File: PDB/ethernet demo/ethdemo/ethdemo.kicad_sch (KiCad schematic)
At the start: 0 parts

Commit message: ad microcontroller and POE+ to demo
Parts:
- added C1: 4.7uF, Capacitor_SMD:C_0603_1608Metric, symbol Device:C
- added C2, C3, C4, C5, C6, C7: 100nF, Capacitor_SMD:C_0603_1608Metric, symbol Device:C
- added C8, C9: 2.2uF, Capacitor_SMD:C_0603_1608Metric, symbol Device:C
- added C83, C84: 0.1uF, Capacitor_SMD:C_0603_1608Metric, symbol Device:C
- added C85: 0.1uF, symbol Device:C
- added C86: 100nf, Capacitor_SMD:C_0603_1608Metric, symbol Device:C
- added D1, D2, D3, D4, D5: LED, LED_SMD:LED_0805_2012Metric, symbol Device:LED
- added D24: 100V, symbol Device:D_Zener
- added D25: 60V, symbol Device:D_Zener
- added F7: Fuse, Fuse:Fuse_1206_3216Metric, symbol Device:Fuse
- added J14: RJ45_Abracon_ARJP11A-MASA-B-A-EMU2, Connector_RJ:RJ45_Abracon_ARJP11A-MA_Horizontal, symbol Connector:RJ45_Abracon_ARJP11A-MASA-B-A-EMU2
- added Q13: CSD19538Q3AT, foot:CSD19538Q3AT, symbol sym&foot:CSD19538Q3AT
- added R10, R6, R7, R8, R9: 270, Resistor_SMD:R_0603_1608Metric, symbol Device:R
- added R73: 22.1Ohm, Resistor_SMD:R_0603_1608Metric, symbol Device:R
- added R74, R75, R76, R77: 1Ohm, Resistor_SMD:R_0603_1608Metric, symbol Device:R
- added R78: 47Ohm, Resistor_SMD:R_0603_1608Metric, symbol Device:R
- added TP1, TP2, TP3, TP4: TestPoint, TestPoint:TestPoint_Pad_D2.5mm, symbol Connector:TestPoint
- added U1: STM32H742VGTx, Package_QFP:LQFP-100_14x14mm_P0.5mm, symbol MCU_ST_STM32H7:STM32H742VGTx
- added U2, U3: LT1117-ADJ, symbol Regulator_Linear:LT1117-ADJ
- added U23: TPS23861PWR, foot:TPS23861PWR, symbol sym&foot:TPS23861PWR
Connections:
- new net: Q13.1 (S_1), Q13.2 (S_2), Q13.3 (S_3), R73.1, R74.1, R75.1, R76.1, R77.1
- new net: R10.1, U1.52 (PB13)
- new net: D5.2 (A), R10.2
- new net: R8.1, U1.45 (PE15)
- new net: D3.2 (A), R8.2
- new net: C85.2, D24.1 (K), D25.2 (A), F7.1, J14.10 (V-), TP4.1
- new net: R6.1, U1.43 (PE13)
- new net: D1.2 (A), R6.2
- new net: R7.1, U1.44 (PE14)
- new net: C8.2, U1.48 (VCAP)
- new net: R9.1, U1.51 (PB12)
- new net: C9.2, U1.73 (VCAP)
- new net: R73.2, U23.15 (SEN1)
- new net: D2.2 (A), R7.2
- new net: C86.2, J14.7
- new net: D4.2 (A), R9.2
- new net: C83.1, U23.1 (VDD), U23.2 (~{RESET}), U23.24 (~{SHTDWN})
- new net: F7.2, Q13.5 (D_1), Q13.6 (D_2), Q13.7 (D_3), Q13.8 (D_4), Q13.D1 (D_5), Q13.D2 (D_6), Q13.D3 (D_7), R78.1
- new net: R78.2, U23.16 (DRAIN1)
- new net: Q13.4 (G), U23.17 (GATE1)
- new net +3.3V: C1.1, C2.1, C3.2, C4.1, C5.1, C6.1, C7.1, TP2.1, U1.100 (VDD), U1.11 (VDD), U1.20 (VREF+), U1.21 (VDDA), U1.27 (VDD), U1.50 (VDD), U1.75 (VDD)
- new net 48V: C84.2, C85.1, D25.1 (K), J14.9 (V+), TP3.1, U23.28 (VPWR)
- new net BOOT0: U1.94 (BOOT0)
- new net CS: U1.28 (PA4)
- new net D+: U1.71 (PA12)
- new net D-: U1.70 (PA11)
- new net GND: C1.2, C2.2, C3.1, C4.2, C5.2, C6.2, C7.2, C8.1, C83.2, C84.1, C86.1, C9.1, D1.1 (K), D2.1 (K), D24.2 (A), D3.1 (K), D4.1 (K), D5.1 (K), R74.2, R75.2, R76.2, R77.2, TP1.1, U1.10 (VSS), U1.19 (VSSA), U1.26 (VSS), U1.49 (VSS), U1.74 (VSS), U1.99 (VSS), U23.11 (KSENSB), U23.12 (SEN4), U23.13 (DRAIN4), U23.18 (KSENSA), U23.19 (SEN2), U23.20 (DRAIN2), U23.22 (AGND), U23.23 (A3), U23.3 (SCL), U23.4 (SDAI), U23.7 (DGND), U23.8 (SEN3), U23.9 (DRAIN3)
- new net INT: U1.67 (PA8)
- new net MISO: U1.30 (PA6)
- new net MOSI: U1.31 (PA7)
- new net PA3: U1.25 (PA3)
- new net PB0: U1.34 (PB0)
- new net PB1: U1.35 (PB1)
- new net PB10: U1.46 (PB10)
- new net PB11: U1.47 (PB11)
- new net PB2: U1.36 (PB2)
- new net PC0: U1.15 (PC0)
- new net PC10: U1.78 (PC10)
- new net PC11: U1.79 (PC11)
- new net PC12: U1.80 (PC12)
- new net PC2: U1.17 (PC2_C)
- new net PC3: U1.18 (PC3_C)
- new net PC4: U1.32 (PC4)
- new net PC5: U1.33 (PC5)
- new net PC8: U1.65 (PC8)
- new net PC9: U1.66 (PC9)
- new net PD2: U1.83 (PD2)
- new net PE11: U1.41 (PE11)
- new net PE12: U1.42 (PE12)
- new net PE7: U1.37 (PE7)
- new net PE8: U1.38 (PE8)
- new net PE9: U1.39 (PE9)
- new net RST: U1.68 (PA9)
- new net SCK: U1.29 (PA5)
- new net SWCLK: U1.76 (PA14)
- new net SWDIO: U1.72 (PA13)
- new net SWO/TRACE: U1.89 (PB3)
- new net UART4_RX: U1.23 (PA1)
- new net UART4_TX: U1.22 (PA0)
- no-connect marks 0 -> 56
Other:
- note added: "TBD"

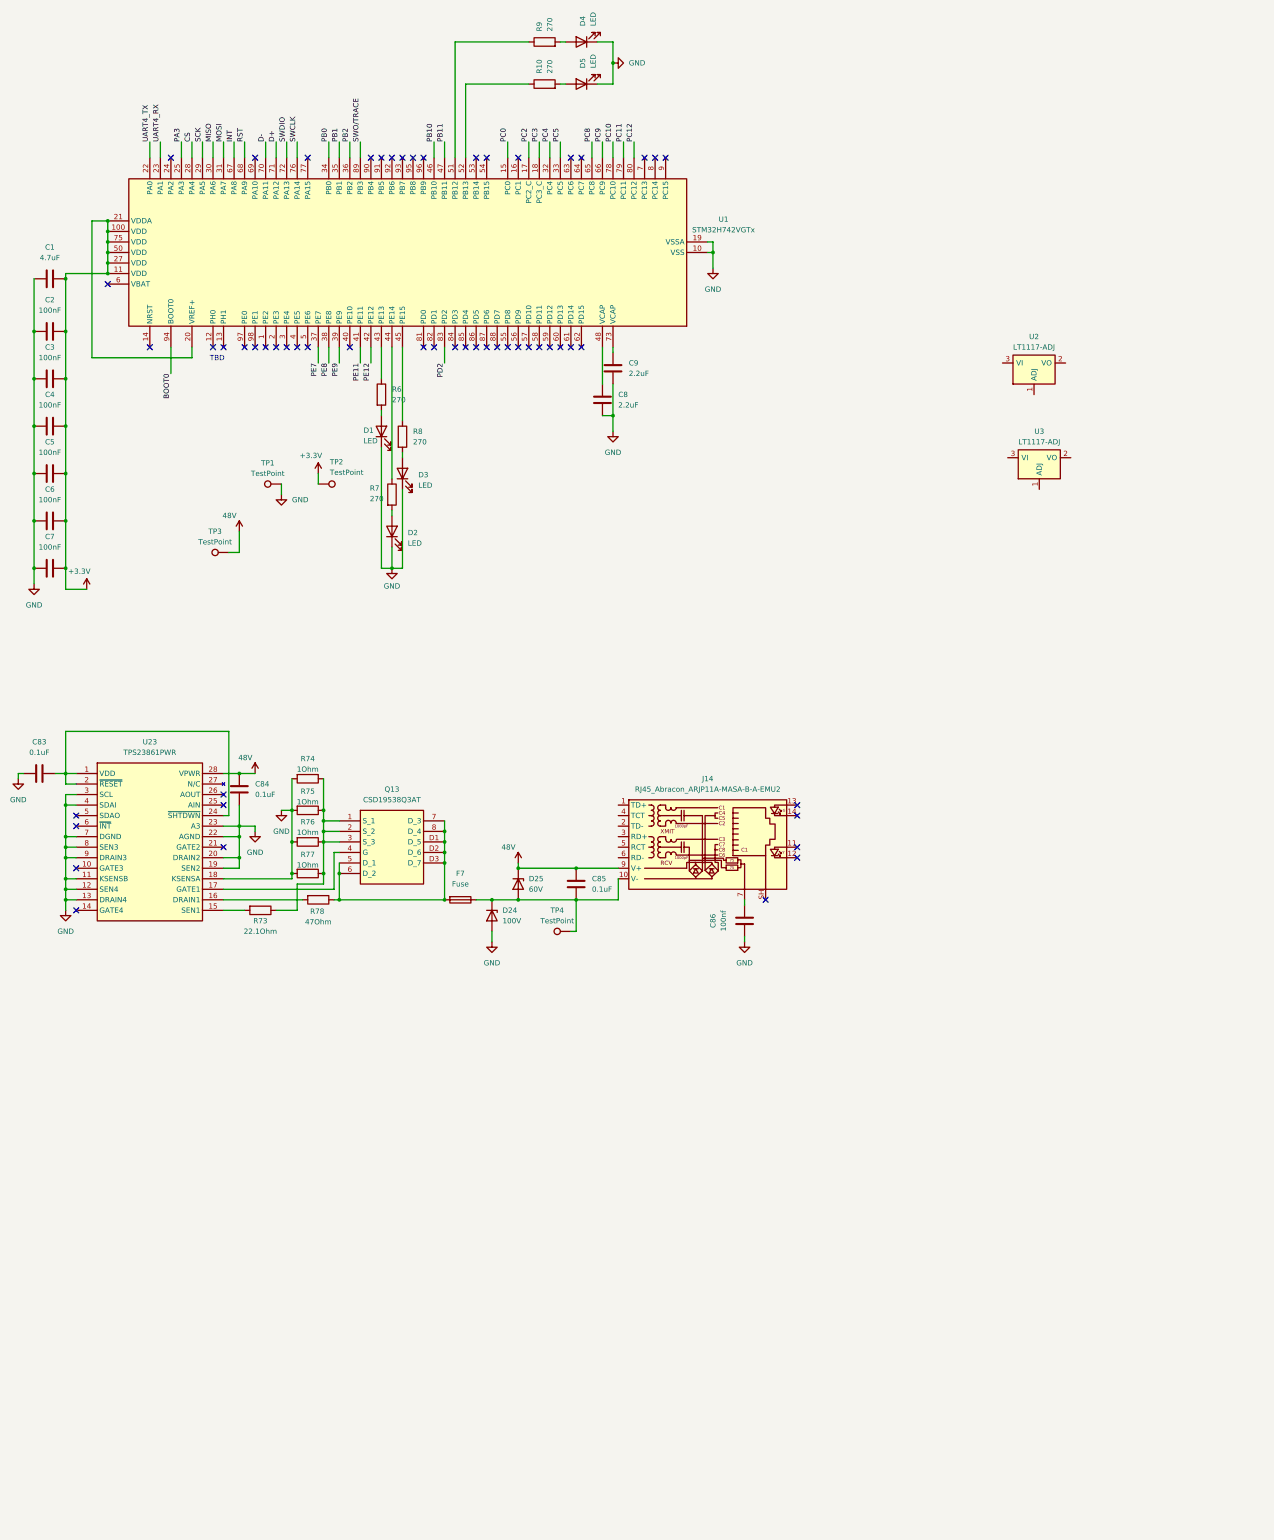
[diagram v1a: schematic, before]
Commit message: added footprints to demo board
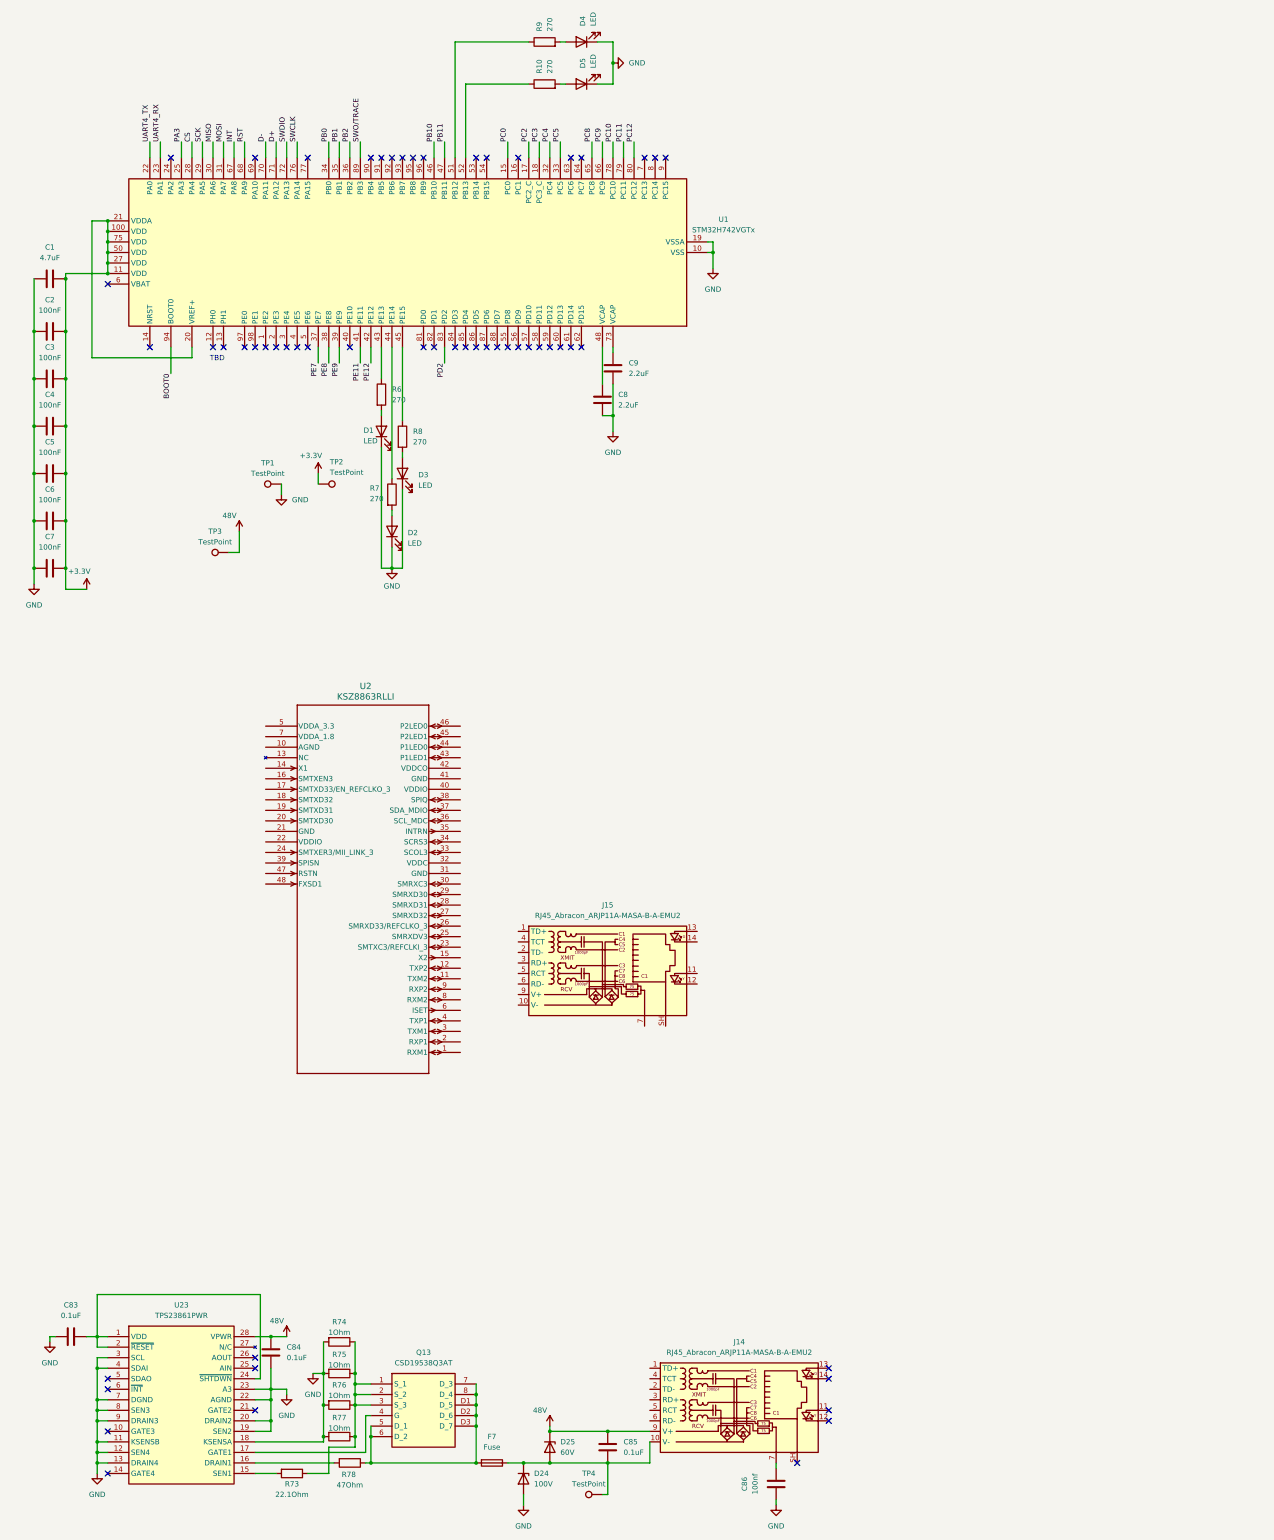
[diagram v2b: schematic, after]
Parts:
- removed U2, U3: LT1117-ADJ, symbol Regulator_Linear:LT1117-ADJ
- added J15: RJ45_Abracon_ARJP11A-MASA-B-A-EMU2, Connector_RJ:RJ45_Abracon_ARJP11A-MA_Horizontal, symbol Connector:RJ45_Abracon_ARJP11A-MASA-B-A-EMU2
- added U2: KSZ8863RLLI, LQFP-48_MCL, symbol sym&foot:KSZ8863RLLI
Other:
- moved on the sheet: C83, C84, C85, C86, D24, D25, F7, J14, Q13, R73, R74, R75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

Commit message: Added PoE+ compliant Magjacks
connect MagJacks to Switch made all terminations, still need to do LED lines
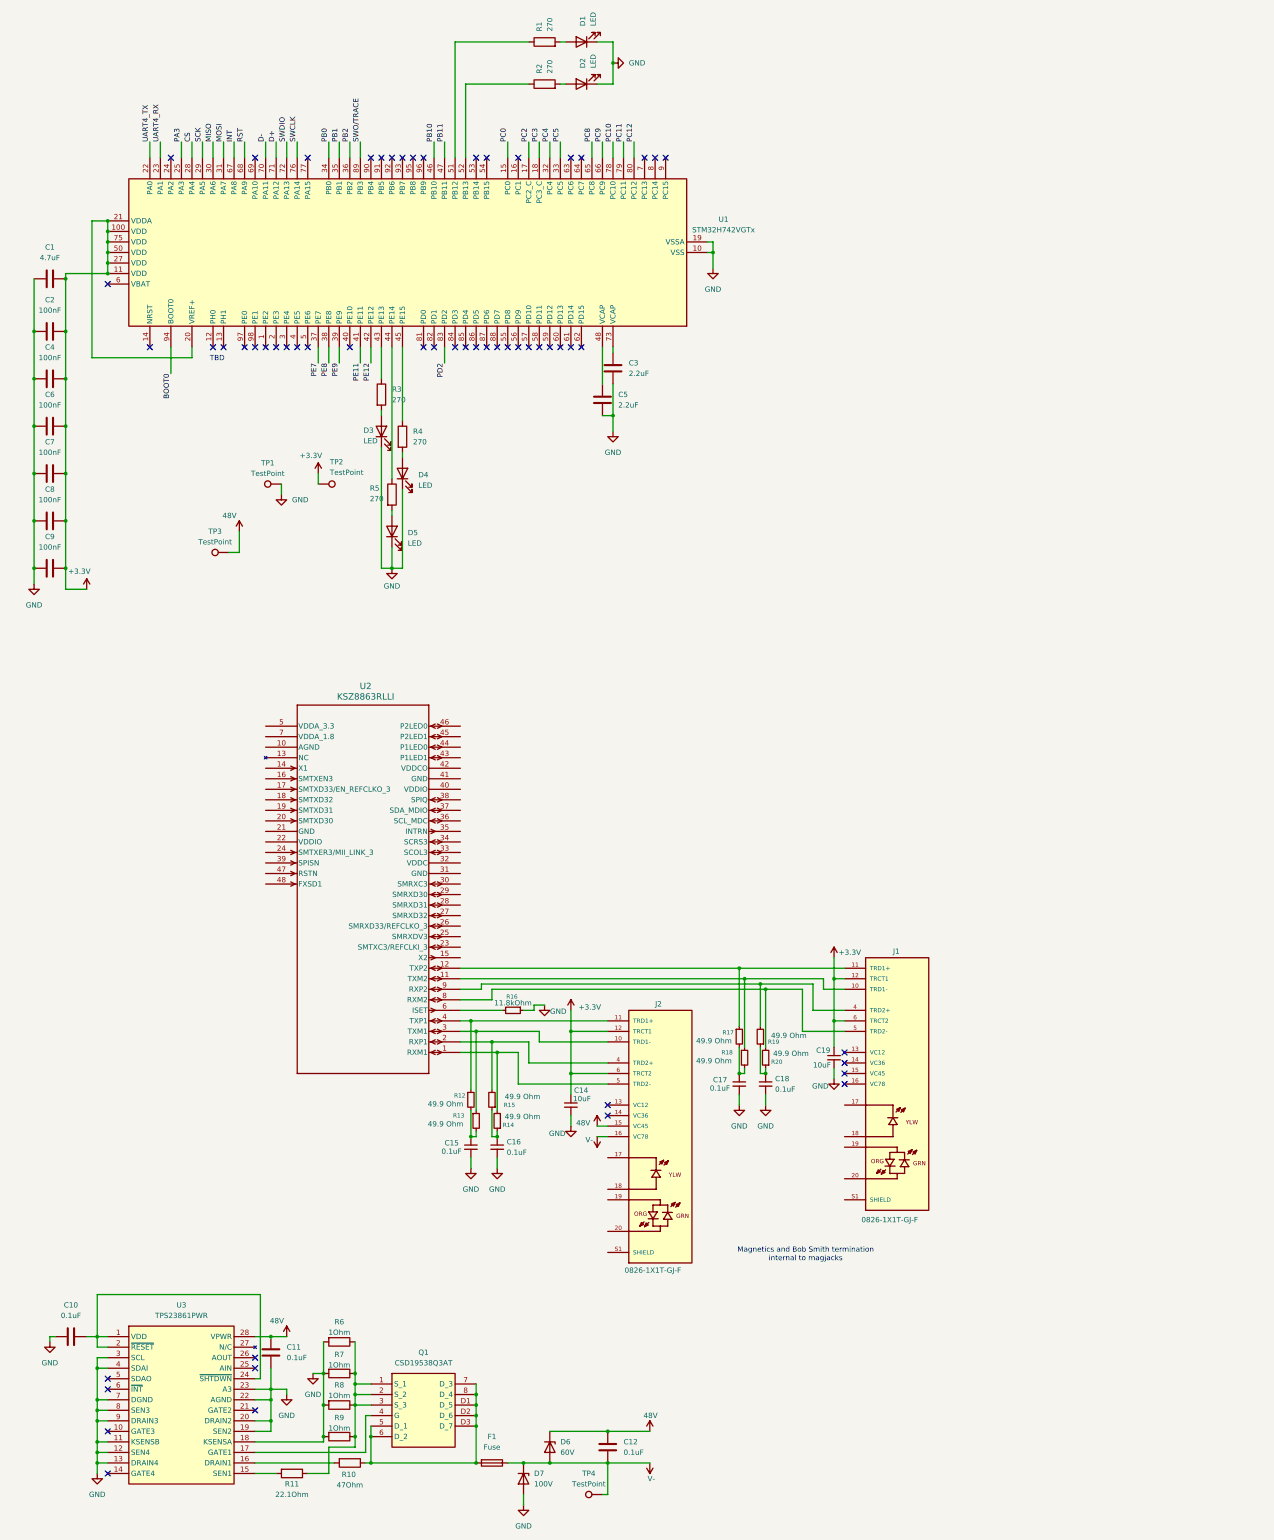
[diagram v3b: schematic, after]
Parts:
- removed C86: 100nf, Capacitor_SMD:C_0603_1608Metric, symbol Device:C
- removed J14, J15: RJ45_Abracon_ARJP11A-MASA-B-A-EMU2, Connector_RJ:RJ45_Abracon_ARJP11A-MA_Horizontal, symbol Connector:RJ45_Abracon_ARJP11A-MASA-B-A-EMU2
- added C14, C19: 10uF, symbol Device:C_Small
- added C15, C16, C17, C18: 0.1uF, symbol Device:C_Small
- added J1, J2: 0826-1X1T-GJ-F, 0826-1X1T-GJ-F:BEL_0826-1X1T-GJ-F, symbol sym&foot:0826-1X1T-GJ-F
- added R12, R13, R14, R15, R17, R18, R19, R20: 49.9 Ohm, symbol Device:R_Small
- added R16: 11.8kOhm, symbol Device:R_Small
- renumbered C83 to C10, C84 to C11, C85 to C12, C9 to C3, C3 to C4, C8 to C5, C4 to C6, C5 to C7, C6 to C8, C7 to C9, D4 to D1, D5 to D2, D1 to D3, D3 to D4, D2 to D5, D25 to D6, D24 to D7, F7 to F1, Q13 to Q1, R9 to R1, R78 to R10, R73 to R11, R10 to R2, R6 to R3, R8 to R4, R7 to R5, R74 to R6, R75 to R7, R76 to R8, R77 to R9, U23 to U3
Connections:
- net +3.3V: now also C14.1, C19.1, J1.12 (TRCT1), J1.6 (TRCT2), J2.12 (TRCT1), J2.6 (TRCT2)
- net 48V: now also J2.15 (VC45)
- net GND: now also C14.2, C15.2, C16.2, C17.2, C18.2, C19.2, R16.1
- net V-: now reaches C12.2, D6.2 (A), D7.1 (K), F1.1, TP4.1
- net V-: now also J2.16 (VC78)
- net at U2.1 (RXM1): now also J2.5 (TRD2-), R14.2
- net at U2.11 (TXM2): now also J1.10 (TRD1-), R18.1
- net at U2.12 (TXP2): now also J1.11 (TRD1+), R17.1
- net at U2.2 (RXP1): now also J2.4 (TRD2+), R15.2
- net at U2.3 (TXM1): now also J2.10 (TRD1-), R13.1
- net at U2.4 (TXP1): now also J2.11 (TRD1+), R12.1
- net at U2.6 (ISET): now also R16.2
- net at U2.8 (RXM2): now also J1.5 (TRD2-), R20.2
- net at U2.9 (RXP2): now also J1.4 (TRD2+), R19.2
- new net: C16.1, R14.1, R15.1
- new net: J1.S1 (SHIELD), J1.S2 (SHIELD)
- new net: C18.1, R19.1, R20.1
- new net: C15.1, R12.2, R13.2
- new net: C17.1, R17.2, R18.2
- new net: J2.S1 (SHIELD), J2.S2 (SHIELD)
- no-connect marks 56 -> 57
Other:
- note added: "Magnetics and Bob Smith termination internal to magjacks"
